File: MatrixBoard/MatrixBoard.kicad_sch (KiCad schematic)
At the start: 77 parts, among them J1 MatrixOut, U1 74HC595, U2 74HC595

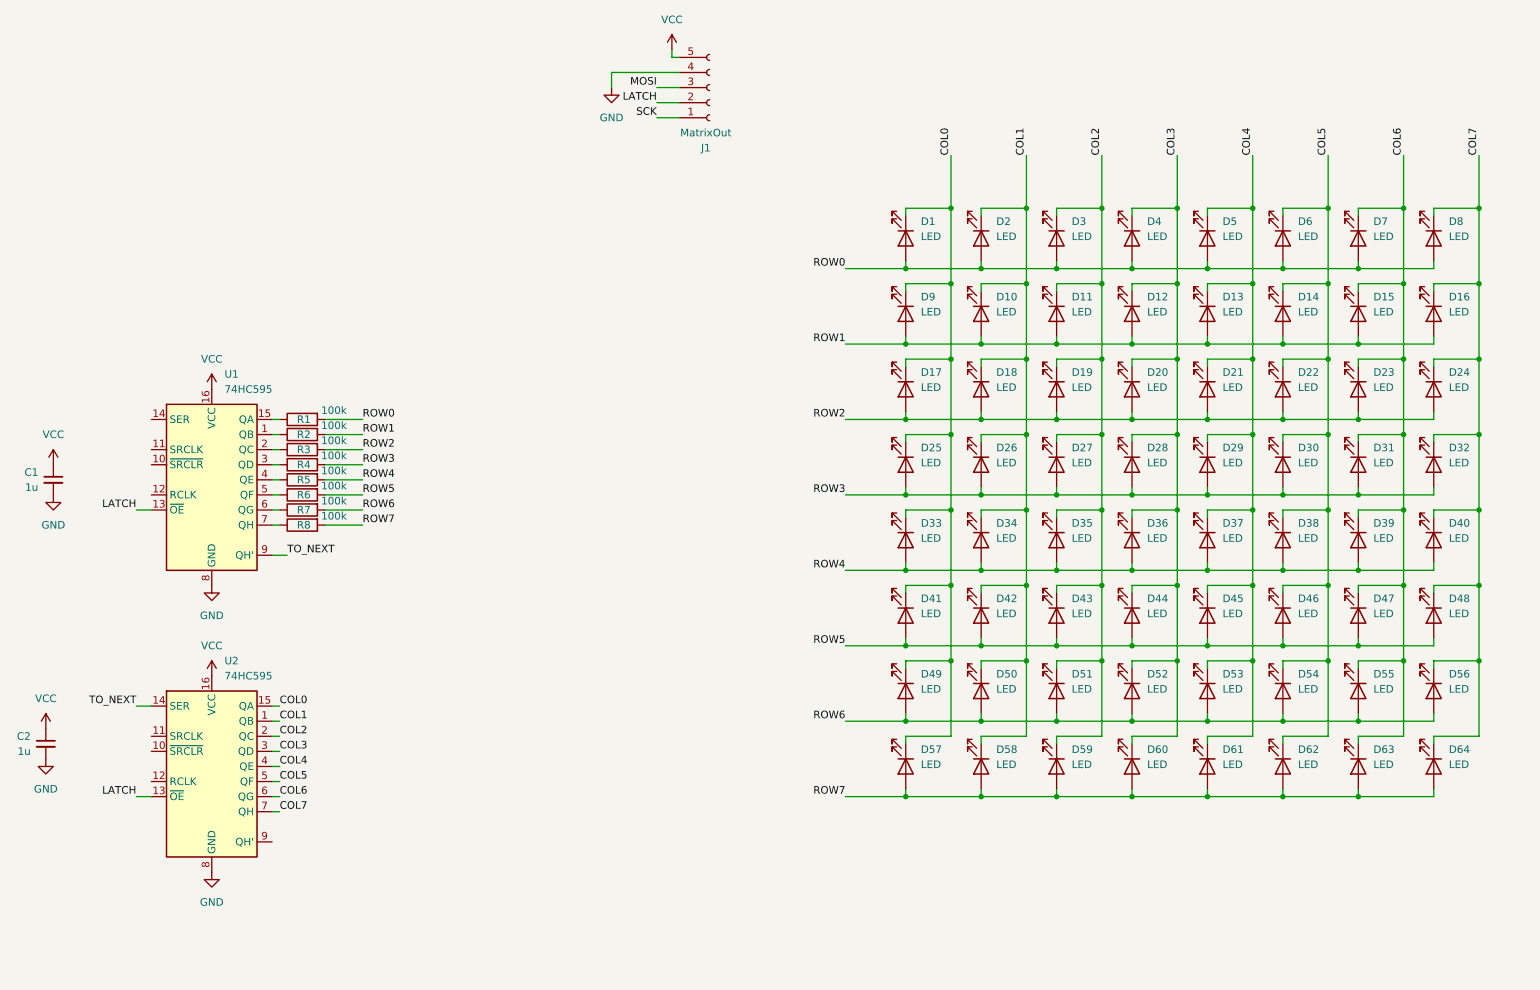
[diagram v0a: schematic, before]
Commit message: add matrix board, change pico to esp32 microcontroller
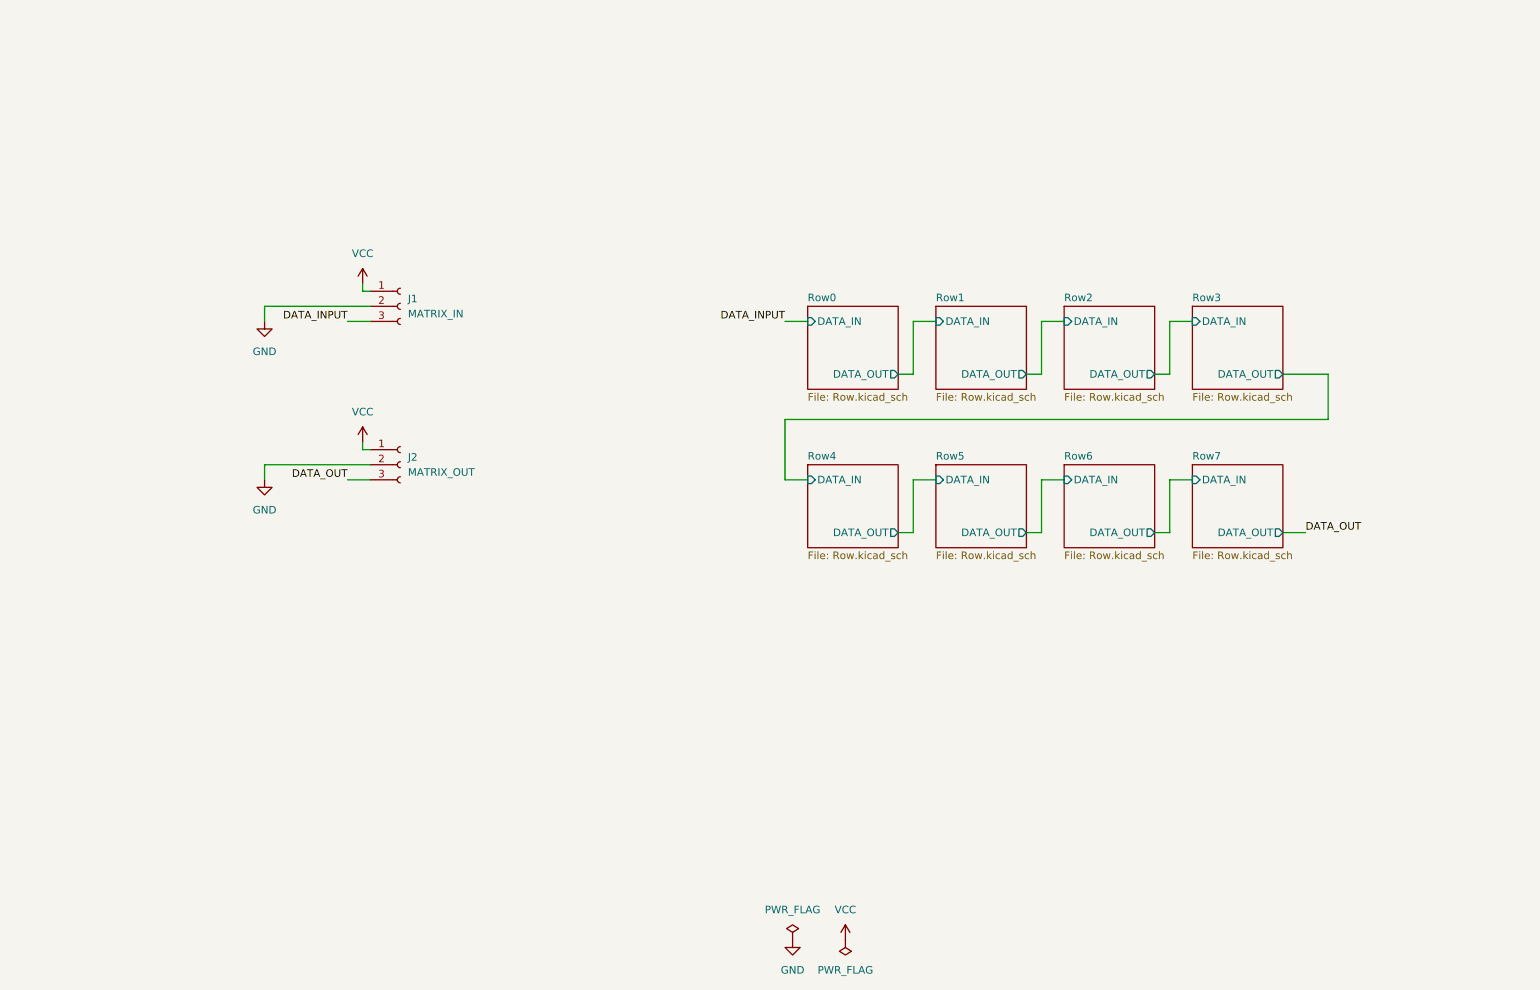
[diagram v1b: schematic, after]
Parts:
- removed C1, C2: 1u, Capacitor_SMD:C_0603_1608Metric_Pad1.08x0.95mm_HandSolder, symbol Device:C_Small
- removed D1, D10, D11, D12, D13, D14, D15, D16, D17, D18, D19, D2, D20, D21, D22, D23, D24, D25, D26, D27, D28, D29, D3, D30, D31, D32, D33, D34, D35, D36, D37, D38, D39, D4, D40, D41, D42, D43, D44, D45, D46, D47, D48, D49, D5, D50, D51, D52, D53, D54, D55, D56, D57, D58, D59, D6, D60, D61, D62, D63, D64, D7, D8, D9: LED, LED_SMD:LED_1206_3216Metric_Pad1.42x1.75mm_HandSolder, symbol Device:LED
- removed J1: MatrixOut, Connector_PinSocket_2.54mm:PinSocket_1x05_P2.54mm_Vertical, symbol Connector:Conn_01x05_Socket
- removed R1, R2, R3, R4, R5, R6, R7, R8: 100k, Resistor_SMD:R_0603_1608Metric_Pad0.98x0.95mm_HandSolder, symbol Device:R
- removed U1, U2: 74HC595, Package_SO:SOP-16_3.9x9.9mm_P1.27mm, symbol 74xx:74HC595
- added J1: MATRIX_IN, Connector_PinHeader_2.54mm:PinHeader_1x03_P2.54mm_Vertical, symbol Connector:Conn_01x03_Socket
- added J2: MATRIX_OUT, Connector_PinHeader_2.54mm:PinHeader_1x03_P2.54mm_Vertical, symbol Connector:Conn_01x03_Socket
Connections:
- net GND: now also J1.2 (Pin_2), J2.2 (Pin_2)
- net VCC: now also J1.1 (Pin_1), J2.1 (Pin_1)
- new net DATA_INPUT: J1.3 (Pin_3)
- new net DATA_OUT: J2.3 (Pin_3)
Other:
- added sheet Row0 (Row.kicad_sch)
- added sheet Row1 (Row.kicad_sch)
- added sheet Row2 (Row.kicad_sch)
- added sheet Row3 (Row.kicad_sch)
- added sheet Row4 (Row.kicad_sch)
- added sheet Row5 (Row.kicad_sch)
- added sheet Row6 (Row.kicad_sch)
- added sheet Row7 (Row.kicad_sch)
- company: (none) -> Miłosz Derżko
- title: (none) -> VirtualBlob

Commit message: add new spring touch
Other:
- company: Miłosz Derżko -> ${Company}
- title: VirtualBlob -> ${ProjectTitle}
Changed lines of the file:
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@@
 	(paper "A4")
 	(title_block
-		(title "VirtualBlob")
+		(title "${ProjectTitle}")
 		(date "2025-11-10")
-		(rev "${revision}")
-		(company "Miłosz Derżko")
+		(rev "${Revision}")
+		(company "${Company}")
 	)
 	(wire

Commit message: Add logo and update project variables
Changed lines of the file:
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@@
 	(title_block
 		(title "${ProjectTitle}")
-		(date "2025-11-10")
+		(date "2025-11-23")
 		(rev "${Revision}")
 		(company "${Company}")
 	)
+	(polyline
+		(pts
+			(xy 269.6902 170.2688) (xy 269.5982 172.845) (xy 268.4389 173.6178) (xy 266.4883 173.5994) (xy 266.5619 169.2751)
+			(xy 268.8805 169.2383) (xy 269.6902 170.2688)
+		)
+		(stroke
+			(width -0.0001)
+			(type solid)
+		)
+		(fill
+			(type outline)
+		)
+	)
+	(polyline
+		(pts
+			(xy 279.4028 169.5727) (xy 279.4028 169.5727)
+		)
+		(stroke
+			(width -0.0001)
+			(type solid)
+		)
+		(fill
+			(type outline)
+		)
+	)
+	(polyline
+		(pts
+			(xy 278.572 174.6695) (xy 278.5781 175.343) (xy 277.7913 175.8842) (xy 277.7133 178.0042) (xy 276.9523 178.0455)
+			(xy 276.9951 175.8919) (xy 276.3531 175.395) (xy 276.3531 174.6664) (xy 278.572 174.6695)
+		)
+		(stroke
+			(width -0.0001)
+			(type solid)
+		)
+		(fill
+			(type outline)
+		)
+	)
+	(polyline
+		(pts
+			(xy 281.2981 170.4927) (xy 280.7277 171.008) (xy 281.3073 171.6244) (xy 281.2981 173.0321) (xy 280.6909 173.6578)
+			(xy 278.8139 173.6762) (xy 278.8323 172.9585) (xy 279.366 172.4065) (xy 278.8047 171.9005) (xy 278.8508 170.1431)
+			(xy 279.4028 169.5727) (xy 280.3597 169.5575) (xy 280.8502 169.548) (xy 281.3165 169.5359) (xy 281.2981 170.4927)
+		)
+		(stroke
+			(width -0.0001)
+			(type solid)
+		)
+		(fill
+			(type outline)
+		)
+	)
+	(polyline
+		(pts
+			(xy 278.1253 171.5784) (xy 278.0891 173.0109) (xy 278.0716 173.494) (xy 278.0563 173.6946) (xy 278.0512 173.701)
+			(xy 278.043 173.7065) (xy 278.0319 173.7111) (xy 278.0181 173.7149) (xy 277.9832 173.7202) (xy 277.9402 173.7228)
+			(xy 277.8906 173.7229) (xy 277.8364 173.7211) (xy 277.7205 173.713) (xy 277.6064 173.7014) (xy 277.5077 173.6894)
+			(xy 277.4123 173.6762) (xy 277.5411 169.5359) (xy 278.1667 169.5175) (xy 278.1253 171.5784)
+		)
+		(stroke
+			(width -0.0001)
+			(type solid)
+		)
+		(fill
+			(type outline)
+		)
+	)
+	(polyline
+		(pts
+			(xy 281.1915 178.1115) (xy 280.671 178.1115) (xy 280.0464 177.2007) (xy 279.604 178.0074) (xy 278.9014 178.0855)
+			(xy 278.9858 174.6969) (xy 279.5323 174.6969) (xy 280.1308 175.5817) (xy 280.6252 174.6188) (xy 281.2758 174.5667)
+			(xy 281.1915 178.1115)
+		)
+		(stroke
+			(width -0.0001)
+			(type solid)
+		)
+		(fill
+			(type outline)
+		)
+	)
+	(polyline
+		(pts
+			(xy 276.1286 169.5035) (xy 276.7911 170.074) (xy 276.7543 171.4541) (xy 275.7054 172.3558) (xy 276.6439 173.6991)
+			(xy 274.0677 173.6991) (xy 274.0884 171.5622) (xy 274.1065 170.0737) (xy 274.1229 169.3563) (xy 276.1286 169.5035)
+		)
+		(stroke
+			(width -0.0001)
+			(type solid)
+		)
+		(fill
+			(type outline)
+		)
+	)
+	(polyline
+		(pts
+			(xy 272.8407 174.5096) (xy 272.8147 177.2941) (xy 272.0248 178.1148) (xy 270.3008 178.1307) (xy 270.3529 177.402)
+			(xy 270.9514 176.9076) (xy 270.3345 176.3308) (xy 270.3221 174.4966) (xy 272.8407 174.5096)
+		)
+		(stroke
+			(width -0.0001)
+			(type solid)
+		)
+		(fill
+			(type outline)
+		)
+	)
+	(polyline
+		(pts
+			(xy 274.1624 174.5556) (xy 275.0472 175.3075) (xy 275.0472 174.5946) (xy 275.8539 174.5686) (xy 275.945 178.0491)
+			(xy 275.1123 178.0751) (xy 274.2106 177.4086) (xy 274.2014 178.0751) (xy 273.4467 178.1271) (xy 273.4337 174.5296)
+			(xy 274.1624 174.5556)
+		)
+		(stroke
+			(width -0.0001)
+			(type solid)
+		)
+		(fill
+			(type outline)
+		)
+	)
+	(polyline
+		(pts
+			(xy 272.8608 169.4299) (xy 273.3392 170.166) (xy 273.284 173.1654) (xy 272.732 173.6991) (xy 270.8366 173.6991)
+			(xy 270.2294 172.9262) (xy 270.3398 170.0924) (xy 271.1127 169.2275) (xy 272.8608 169.4299)
+		)
+		(stroke
+			(width -0.0001)
+			(type solid)
+		)
+		(fill
+			(type outline)
+		)
+	)
+	(polyline
+		(pts
+			(xy 269.6944 175.2113) (xy 269.0438 175.7057) (xy 269.6944 176.1742) (xy 269.6684 177.6533) (xy 269.0699 178.2779)
+			(xy 266.5976 178.3039) (xy 266.6236 177.5492) (xy 267.2117 177.0193) (xy 266.6328 176.5416) (xy 266.6389 175.1737)
+			(xy 267.2742 174.5045) (xy 269.6944 174.5044) (xy 269.6944 175.2113)
+		)
+		(stroke
+			(width -0.0001)
+			(type solid)
+		)
+		(fill
+			(type outline)
+		)
+	)
 	(wire
